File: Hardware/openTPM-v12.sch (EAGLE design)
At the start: 65 parts, among them U1 SAM4S4A, U2 TPS62172, X1 TC2050-NL-MCP-NL, Y1 12MHZ, Y2 32KHz

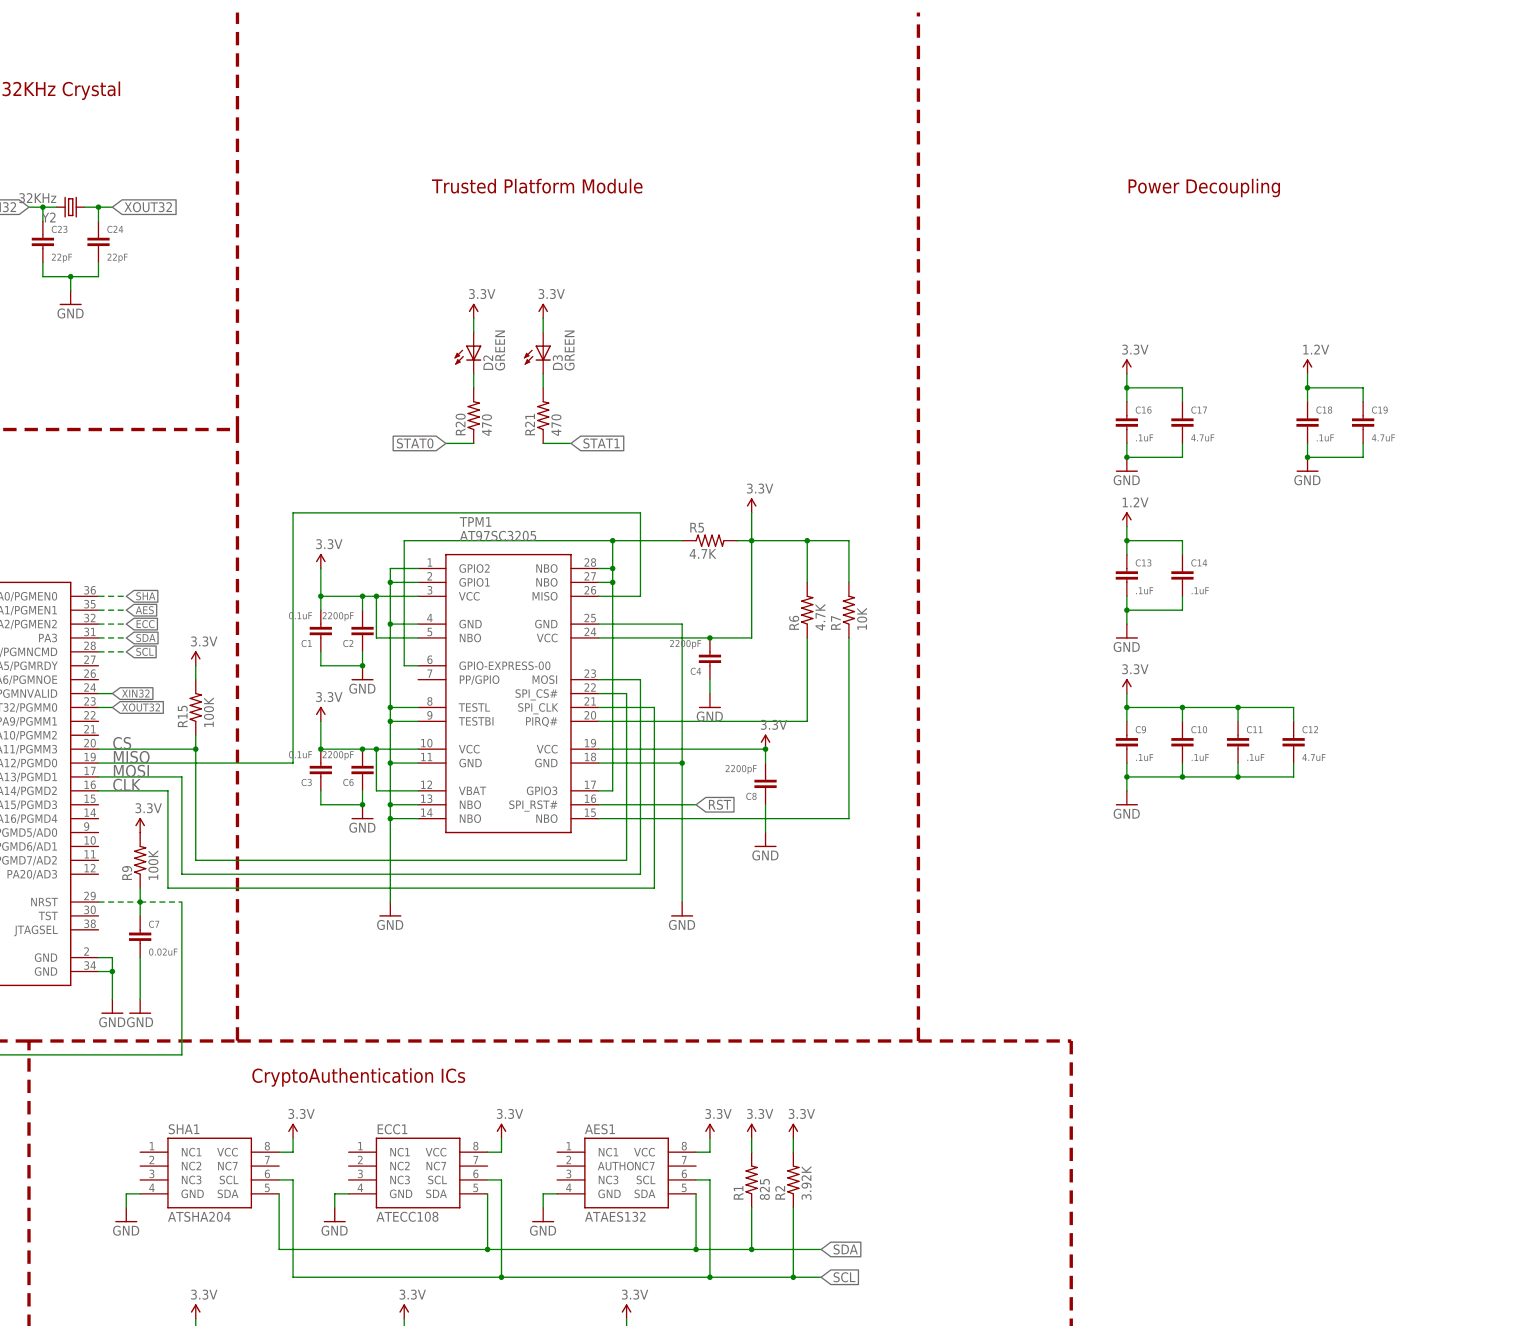
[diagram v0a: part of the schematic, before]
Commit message: reorg of images, update to board trace widths for power, added to gitignore
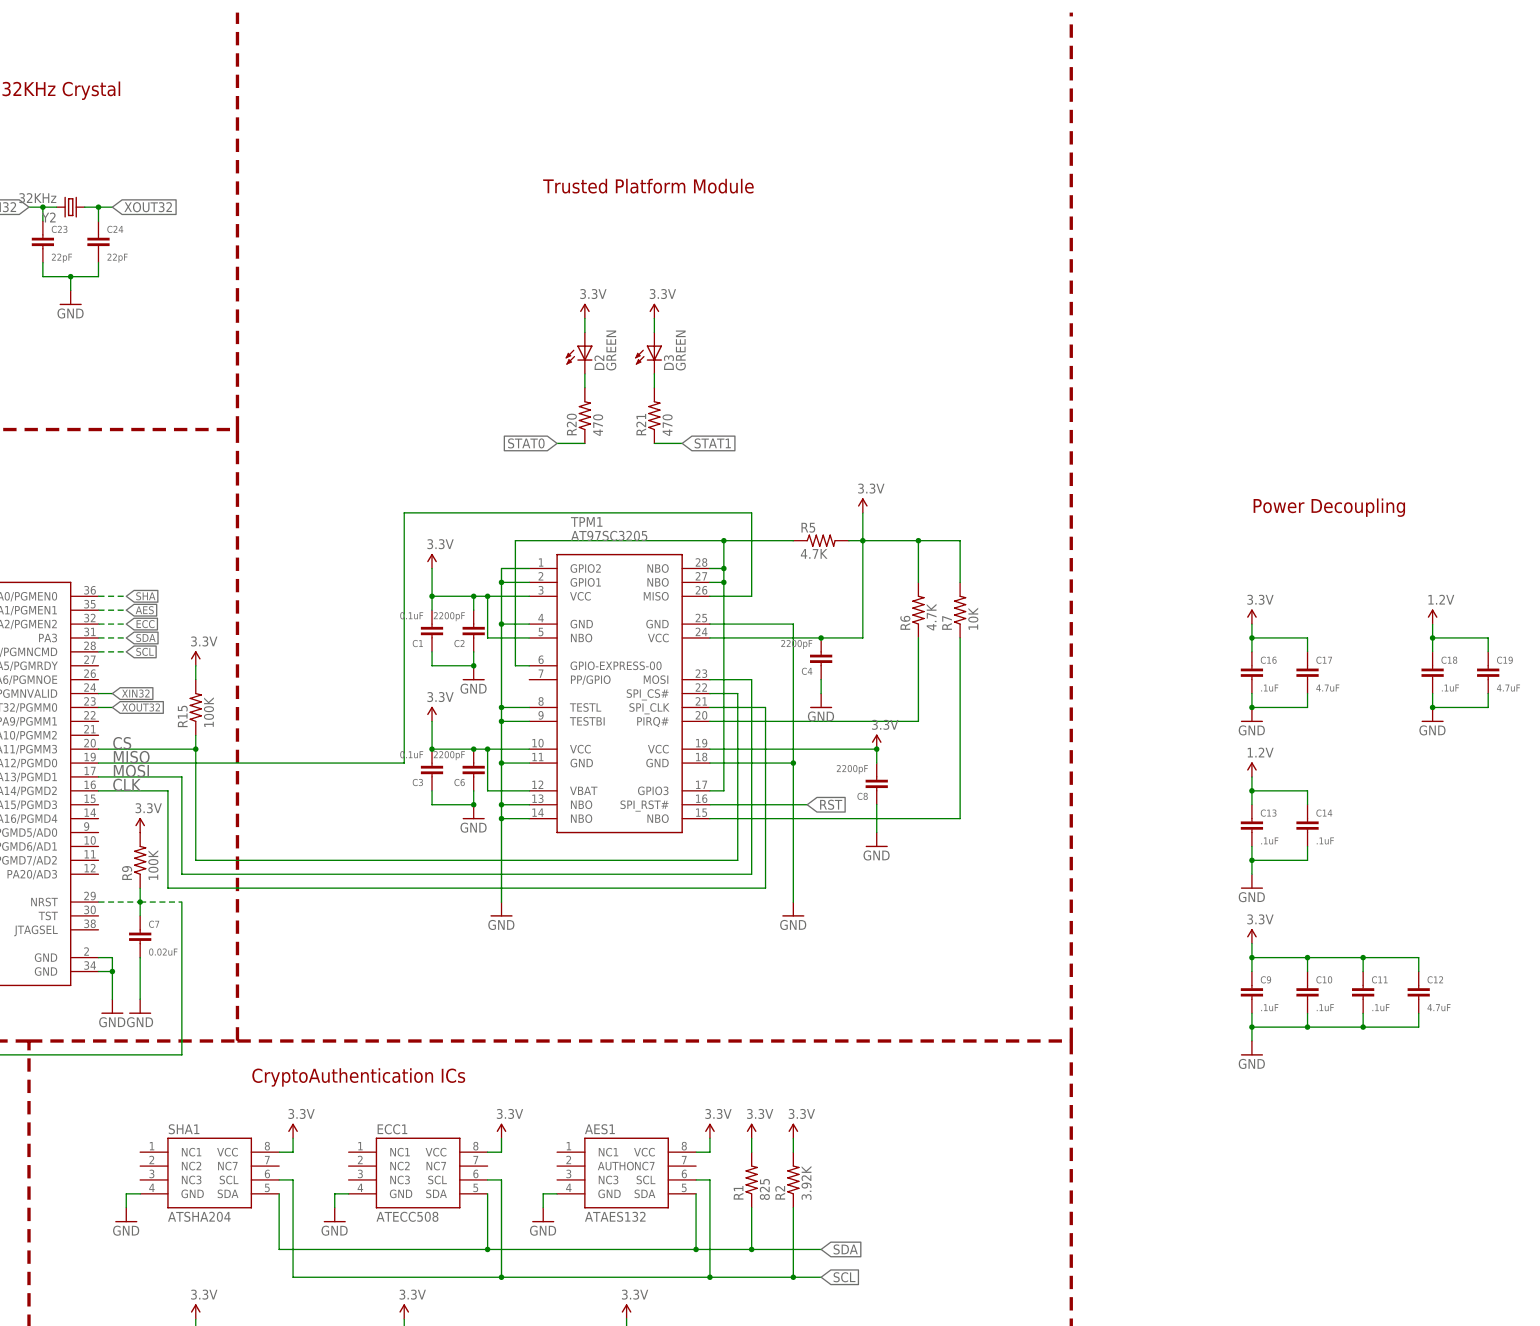
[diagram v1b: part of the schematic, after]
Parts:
- ECC1: value ATECC108 -> ATECC508; device TPM:CRYPTOTRONIX_ATECC108 -> TPM:ATECC508
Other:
- moved on the sheet: C1, C10, C11, C12, C13, C14, C16, C17, C18, C19, C2, C3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
